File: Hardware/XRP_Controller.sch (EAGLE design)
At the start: 109 parts, among them J1 POWER_JACKPOWER_JACK_SLOT, J12 Vertical Qwiic Connector, J13 Vertical Qwiic Connector, J14 Vertical Qwiic Connector, J3 JST_6_PIN_VERTICAL, J4 JST_6_PIN_VERTICAL, J5 JST_6_PIN_VERTICAL, J6 JST_6_PIN_VERTICAL, J9 Vertical Qwiic Connector, Q3 20V/4.2A/52mΩ/1.4W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

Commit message: Design review updates
Move version number in schematic to correct location
Rename 2nd expansion connector from "Range" to "Extra"
Rename 4th expansion connector from "Conn4" to "Range"
Add VIN measurement through voltage divider and NC jumper to IO28
Add V_BATT test point
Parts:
- added R15: 33k, SparkFun-Resistors:33KOHM-0603-1/10W-1%
- added R16: 100k, SparkFun-Resistors:100KOHM-0603-1/10W-1%
- added TP37: TEST-POINT3X5, SparkFun-Connectors:TEST-POINT3X5
- added VIN_MEAS: JUMPER-SMT_2_NC_TRACE_SILK, SparkFun-Jumpers:JUMPER-SMT_2_NC_TRACE_SILK
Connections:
- new net N$12: R15.2, R16.1, VIN_MEAS.2
- net GND: now also R15.1
- net RP_IO28: now also VIN_MEAS.1
- net VIN: now also R16.2
- net V_BATT: now also TP37.1
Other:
- note added: "Cut VIN_MEAS jumper to disconnect from IO28"
- note added: "VIN Measurement"
- moved on the sheet: I2C, R1, R2, TP34, TP35, TP36

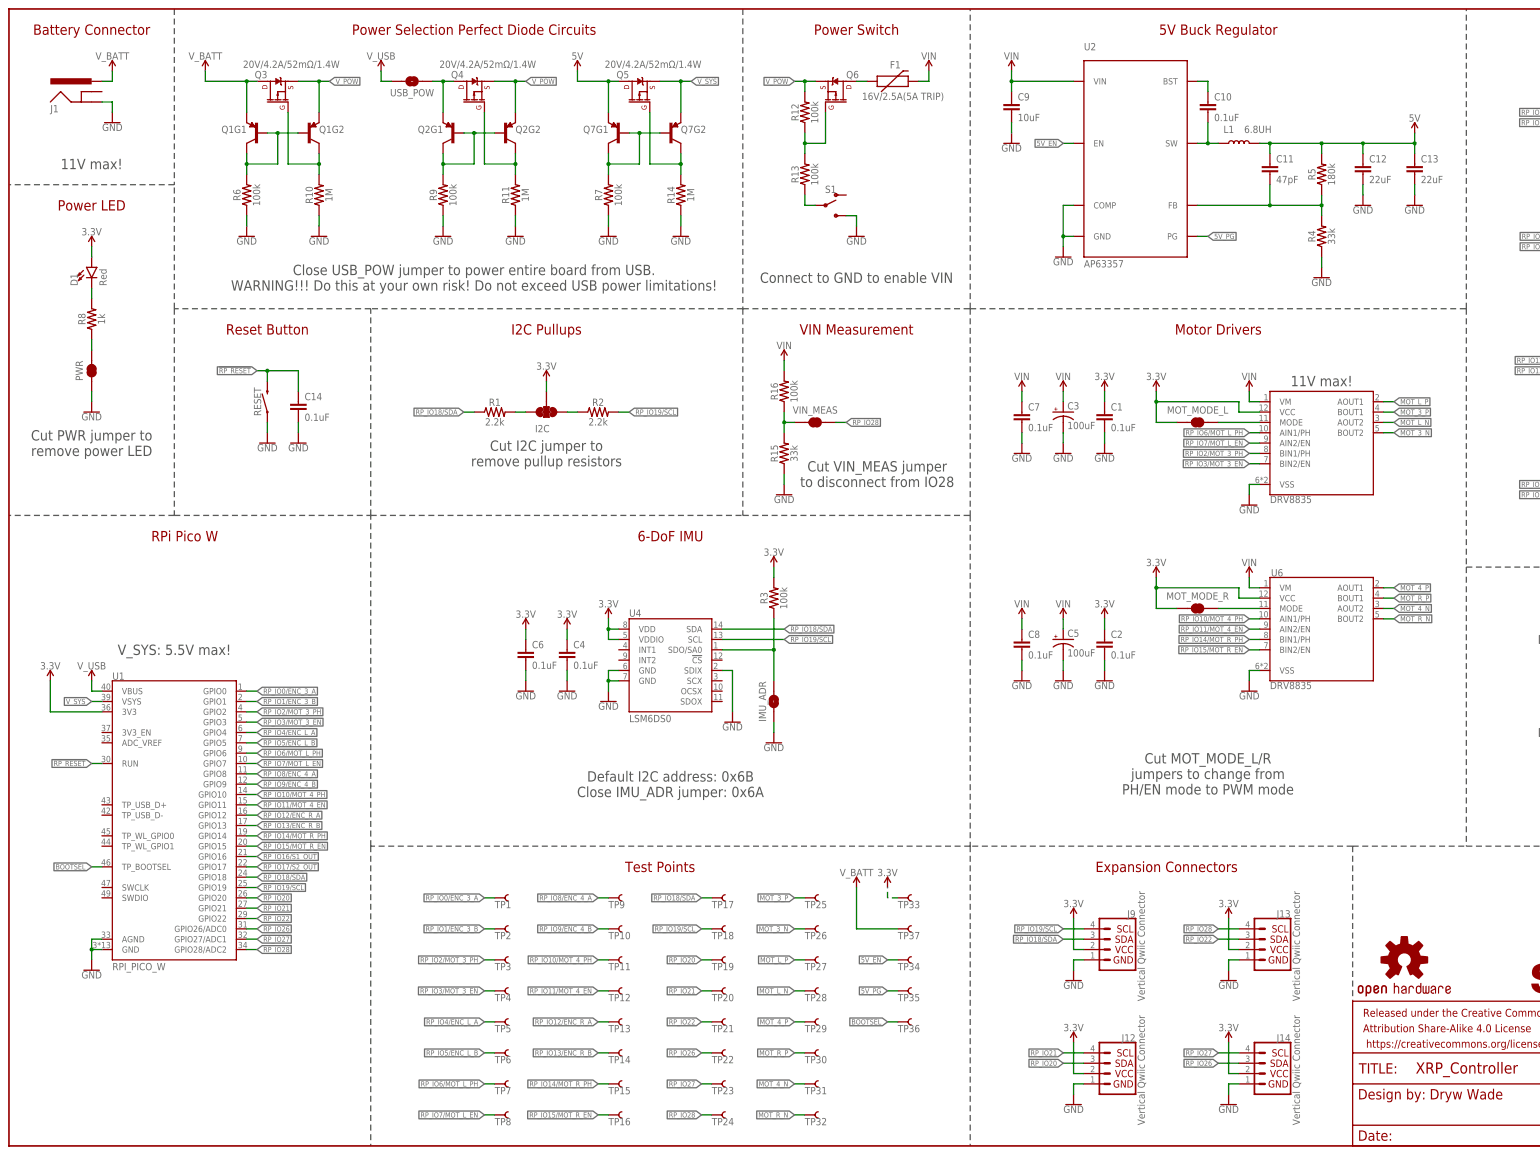
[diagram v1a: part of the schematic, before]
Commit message: Design review updates
Schematic:
Restore Q6 value
Add user button to IO22 via NC jumper
Move USB_POW next to Pico W
Add current limiting resistor to VUSB

Board:
Place user button at top left corner
Move USB_POW jumper under barrel connector
Nudge V_SYS trace to get better GND pour
Reduce selective solder path widths
Move test points away from middle to make room for logos (BOOTSEL, V_BATT, 3.3V, MOT_3_PH/EN)
Add vias to power traces for less voltage drop
Update vertical Qwiic connector footprint
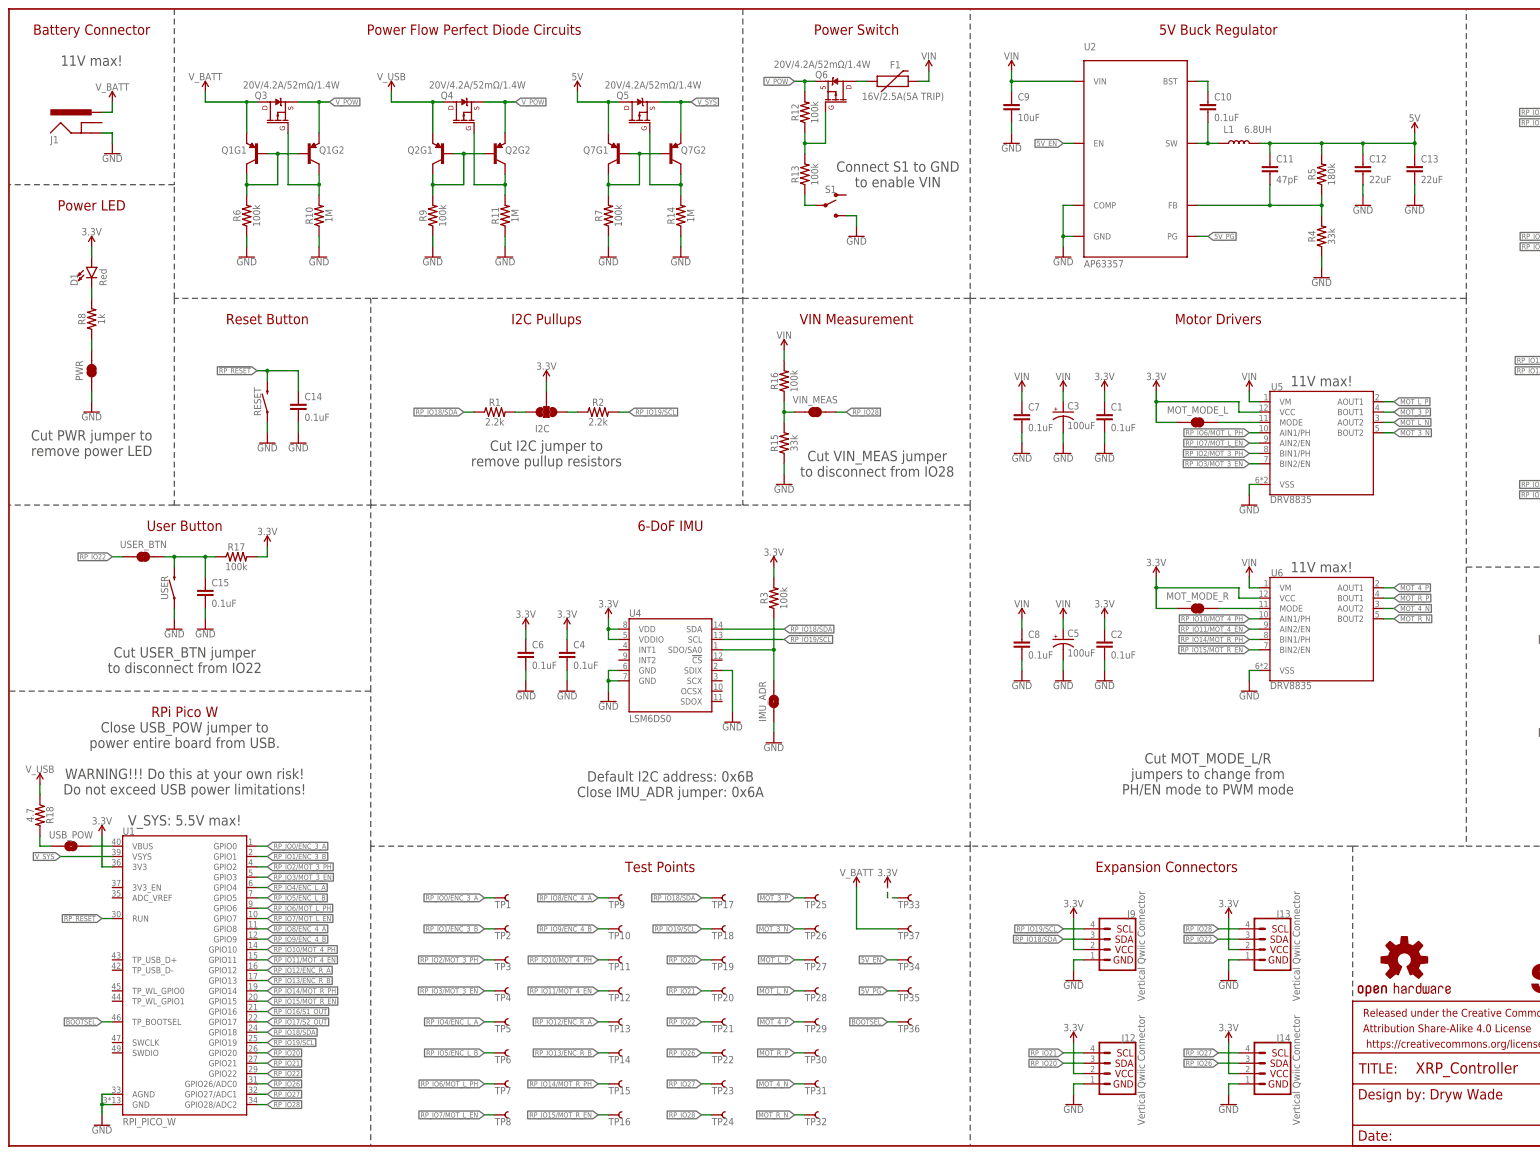
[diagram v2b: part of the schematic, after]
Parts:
- added C15: 0.1uF, SparkFun-Capacitors:0.1UF-0603-25V-(+80/-20%)
- added R17: 100k, SparkFun-Resistors:100KOHM-0603-1/10W-1%
- added R18: 4.7, SparkFun-Resistors:4.7OHM-0603-1/10W-1%
- added USER: MOMENTARY-SWITCH-SPST-SMD-4.6X2.8MM, SparkFun-Switches:MOMENTARY-SWITCH-SPST-SMD-4.6X2.8MM
- added USER_BTN: JUMPER-SMT_2_NC_TRACE_SILK, SparkFun-Jumpers:JUMPER-SMT_2_NC_TRACE_SILK
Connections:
- new net N$17: C15.1, R17.1, USER.2, USER_BTN.1
- new net N$18: R18.2, USB_POW.2
- net 3.3V: now also R17.2
- net GND: now also C15.2, USER.1
- net N$9: now also U1.VBUS, USB_POW.1; no longer Q2G1.E, Q4.D, USB_POW.2
- net RP_IO22: now also USER_BTN.2
- net V_USB: now also Q2G1.E, Q4.D, R18.1; no longer U1.VBUS, USB_POW.1
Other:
- note added: "Close USB_POW jumper to power entire board from USB. WARNING!!! Do this at your own risk! Do not exceed USB power limitations! V_SYS: 5.5V max!"
- note added: "Connect S1 to GND to enable VIN"
- note added: "Cut USER_BTN jumper to disconnect from IO22"
- note added: "Power Flow Perfect Diode Circuits"
- note added: "User Button"
- note removed: "Close USB_POW jumper to power entire board from USB. WARNING!!! Do this at your own risk! Do not exceed USB power limitations!"
- note removed: "Connect to GND to enable VIN"
- note removed: "Power Selection Perfect Diode Circuits"
- note removed: "V_SYS: 5.5V max!"
- moved on the sheet: J1, Q1G1, Q1G2, Q2G1, Q2G2, Q3, Q4, Q5, Q7G1, Q7G2, R10, R11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

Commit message: v10 updates
Bump version number to v10
Update Pico W datasheet
Change Pico W footprint to match datasheet recommendations
Nudge inner expansion connectors inwards to be on 0.05" grid
Rename USB_POW jumper to VUSB
Replace PWR_LED jumper silk label with PWR
Add XRP logos
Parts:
- LOGO3: value SFE_LOGO_NAME_FLAME.1_INCH -> SFE_LOGO_NAME_FLAME.3_INCH; device SparkFun-Aesthetics:SFE_LOGO_NAME_FLAME.1_INCH -> SparkFun-Aesthetics:SFE_LOGO_NAME_FLAME.3_INCH
- renumbered USB_POW to VUSB
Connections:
- net RP_IO20 renamed RP_IO20/RANGE_TRIG
- net RP_IO21 renamed RP_IO21/RANGE_ECHO
- net RP_IO22 renamed RP_IO22/USER_BTN
- net RP_IO26 renamed RP_IO26/LINE_L
- net RP_IO27 renamed RP_IO27/LINE_R
- net RP_IO28 renamed RP_IO28/VIN_MEAS
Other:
- note added: "Close VUSB jumper to power entire board from USB. WARNING!!! Do this at your own risk! Do not exceed USB power limitations! V_SYS: 5.5V max!"
- note added: "v10"
- note removed: "Close USB_POW jumper to power entire board from USB. WARNING!!! Do this at your own risk! Do not exceed USB power limitations! V_SYS: 5.5V max!"
- note removed: "v02"
- moved on the sheet: TP1, TP17, TP18, TP19, TP2, TP20, TP21, TP22, TP23, TP24, TP25, TP26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

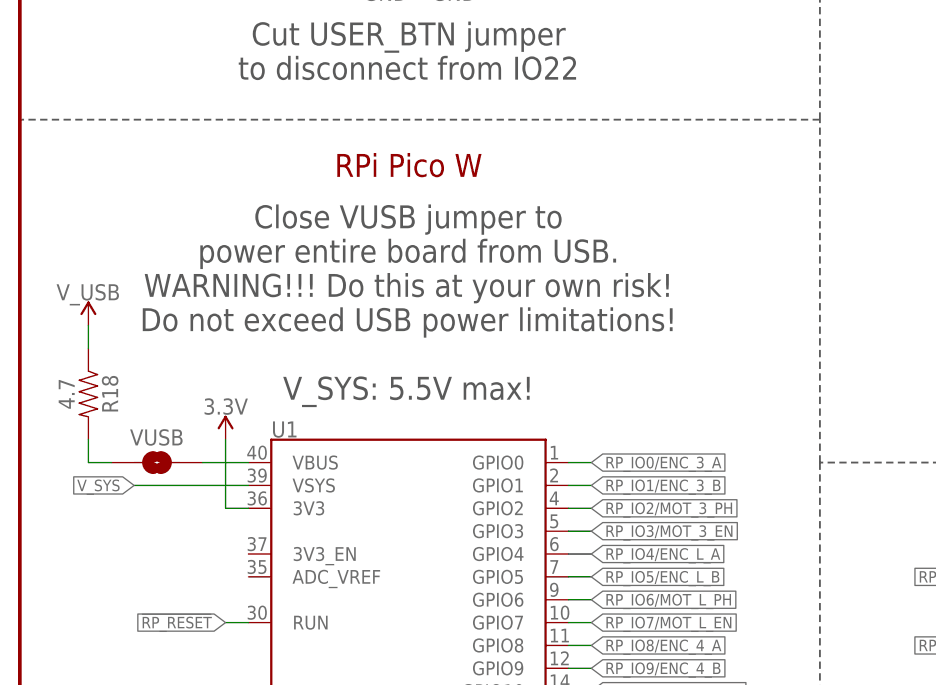
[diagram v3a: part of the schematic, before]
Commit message: Update VUSB path
Replace R18 with 2x 1206 10 Ohm resistors in parallel (better power rating than a single 0603)
Change VUSB jumper from NO to NC
Flip 3V3 and VBUS pins of Pico W footprint
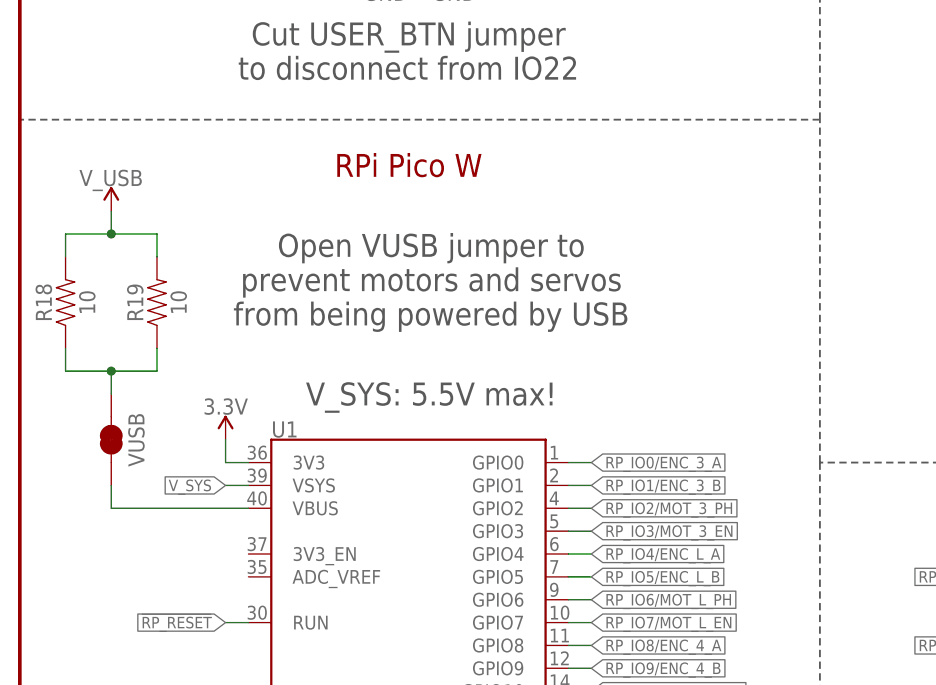
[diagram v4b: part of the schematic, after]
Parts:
- added R19: 10, SparkFun-Resistors:10OHM-1206-1/4W-1%
- R18: value 4.7 -> 10; device SparkFun-Resistors:4.7OHM-0603-1/10W-1% -> SparkFun-Resistors:10OHM-1206-1/4W-1%
- VUSB: value JUMPER-SMT_2_NO_SILK -> JUMPER-SMT_2_NC_TRACE_SILK; device SparkFun-Jumpers:JUMPER-SMT_2_NO_SILK -> SparkFun-Jumpers:JUMPER-SMT_2_NC_TRACE_SILK
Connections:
- net N$18: now also R18.1, R19.1; no longer R18.2
- net V_USB: now also R18.2, R19.2; no longer R18.1
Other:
- note added: "Open VUSB jumper to prevent motors and servos from being powered by USB"
- note added: "V_SYS: 5.5V max!"
- note removed: "Close VUSB jumper to power entire board from USB. WARNING!!! Do this at your own risk! Do not exceed USB power limitations! V_SYS: 5.5V max!"
- moved on the sheet: R18

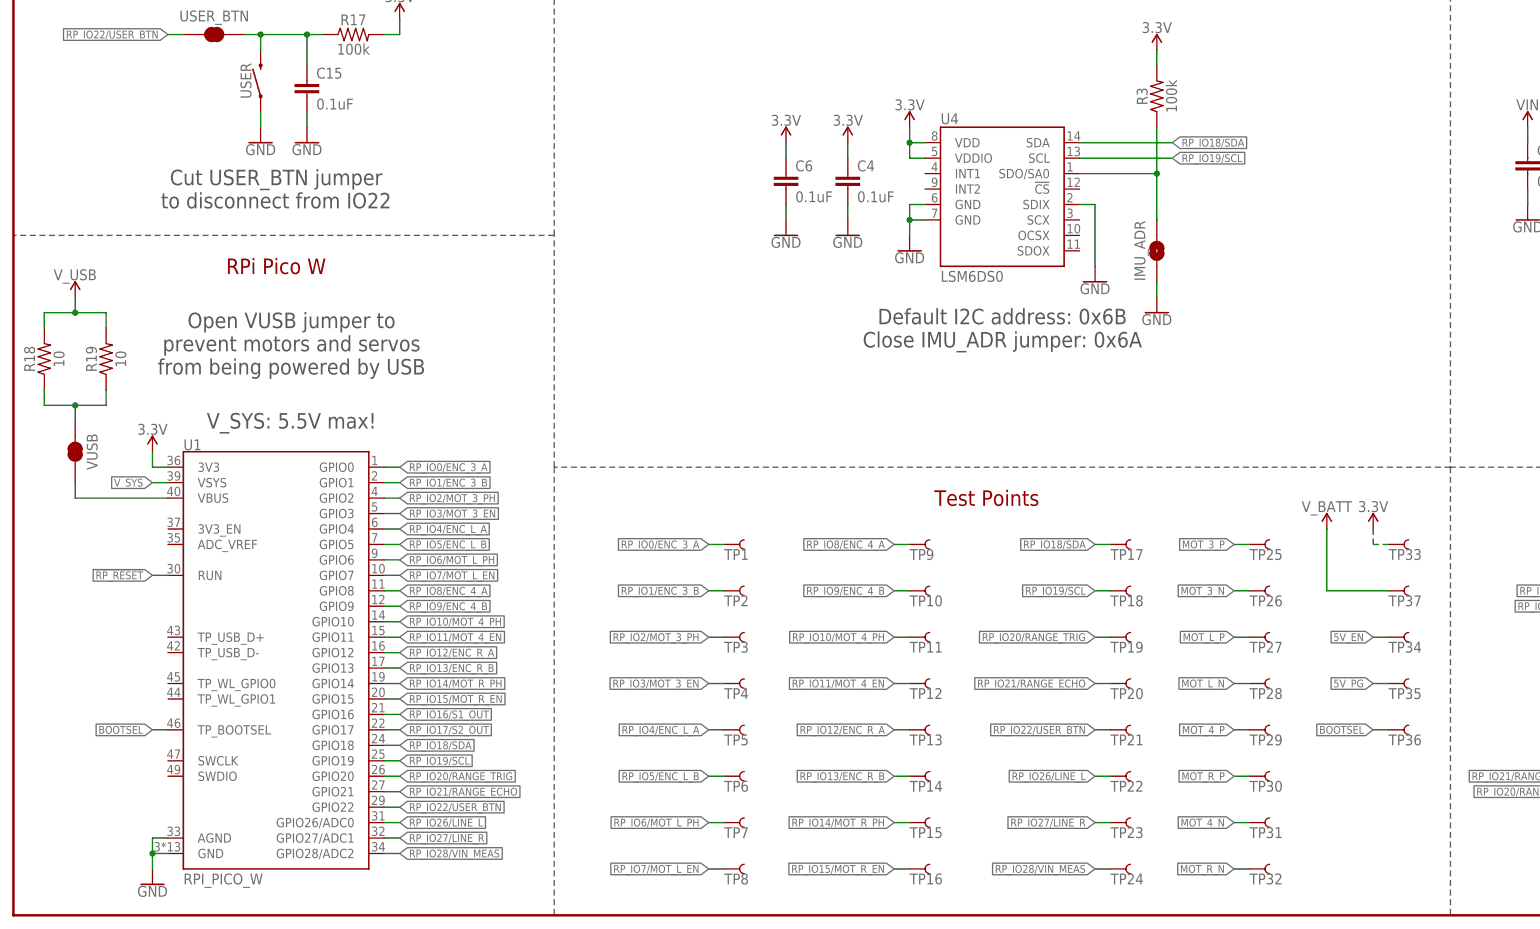
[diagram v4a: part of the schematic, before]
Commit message: Design review updates
Add IO22 silk label to user button
Move VUSB jumper under V_SYS label in schematic
Renumber last few test points
Add test point for IMU interrupt pin
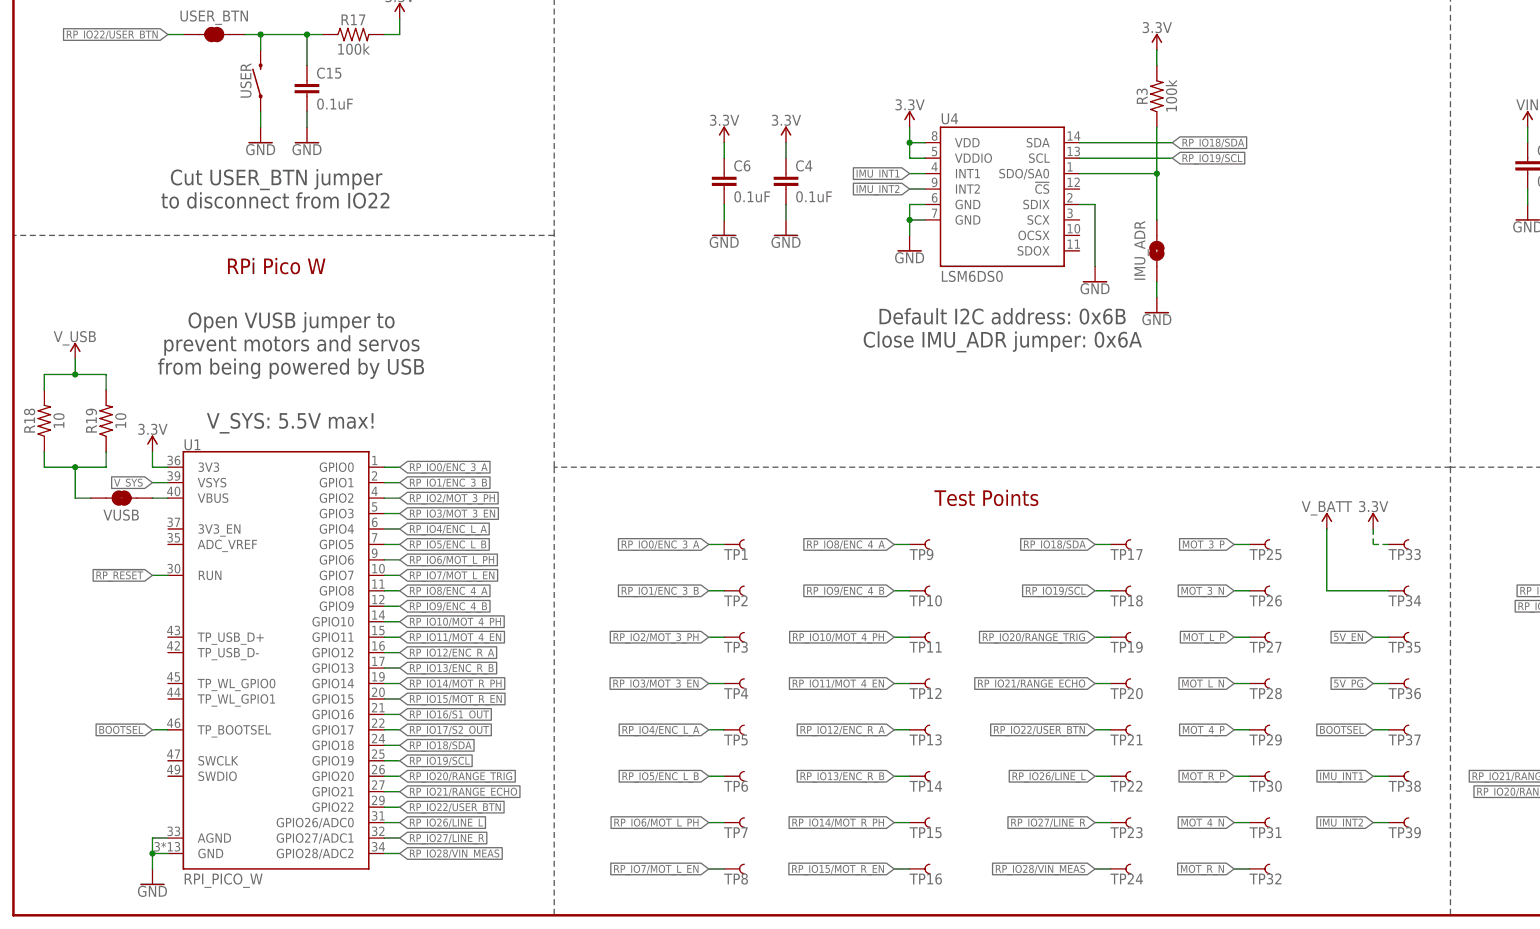
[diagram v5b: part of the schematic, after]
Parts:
- added TP38, TP39: TEST-POINT3X5, SparkFun-Connectors:TEST-POINT3X5
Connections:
- new net IMU_INT1: TP38.1, U4.INT1
- new net IMU_INT2: TP39.1, U4.INT2
- net 5V_EN: now also TP35.1; no longer TP34.1
- net 5V_PG: now also TP36.1; no longer TP35.1
- net BOOTSEL: now also TP37.1; no longer TP36.1
- net N$18: now also VUSB.1; no longer VUSB.2
- net N$9: now also VUSB.2; no longer VUSB.1
- net V_BATT: now also TP34.1; no longer TP37.1
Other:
- moved on the sheet: C4, C6, R18, R19, TP34, TP35, TP36, TP37, VUSB

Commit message: Connect SCX pin of IMU to GND
Datasheet says to do this, whoops!
Pins 10-12 have internal pullups, can leave unconnected
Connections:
- net GND: now also U4.SCX
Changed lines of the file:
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@@
 <pinref part="GND13" gate="1" pin="GND"/>
 <pinref part="U4" gate="G$1" pin="SDIX"/>
-<wire x1="177.8" y1="106.68" x2="177.8" y2="116.84" width="0.1524" layer="91"/>
+<wire x1="177.8" y1="106.68" x2="177.8" y2="114.3" width="0.1524" layer="91"/>
+<wire x1="177.8" y1="114.3" x2="177.8" y2="116.84" width="0.1524" layer="91"/>
 <wire x1="177.8" y1="116.84" x2="175.26" y2="116.84" width="0.1524" layer="91"/>
+<pinref part="U4" gate="G$1" pin="SCX"/>
+<wire x1="175.26" y1="114.3" x2="177.8" y2="114.3" width="0.1524" layer="91"/>
+<junction x="177.8" y="114.3"/>
 </segment>
 <segment>
